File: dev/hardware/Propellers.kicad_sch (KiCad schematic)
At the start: 25 parts, among them J201 CPU PGMR, J202 GPU PGMR, J203 SPARE GPU HDR, J204 SPARE CPU HDR, SW201 CPU ~{RES}, SW202 GPU ~{RES}, SW203 DEBUG, U1 P8X32A-D40, Y1 6.5MHz

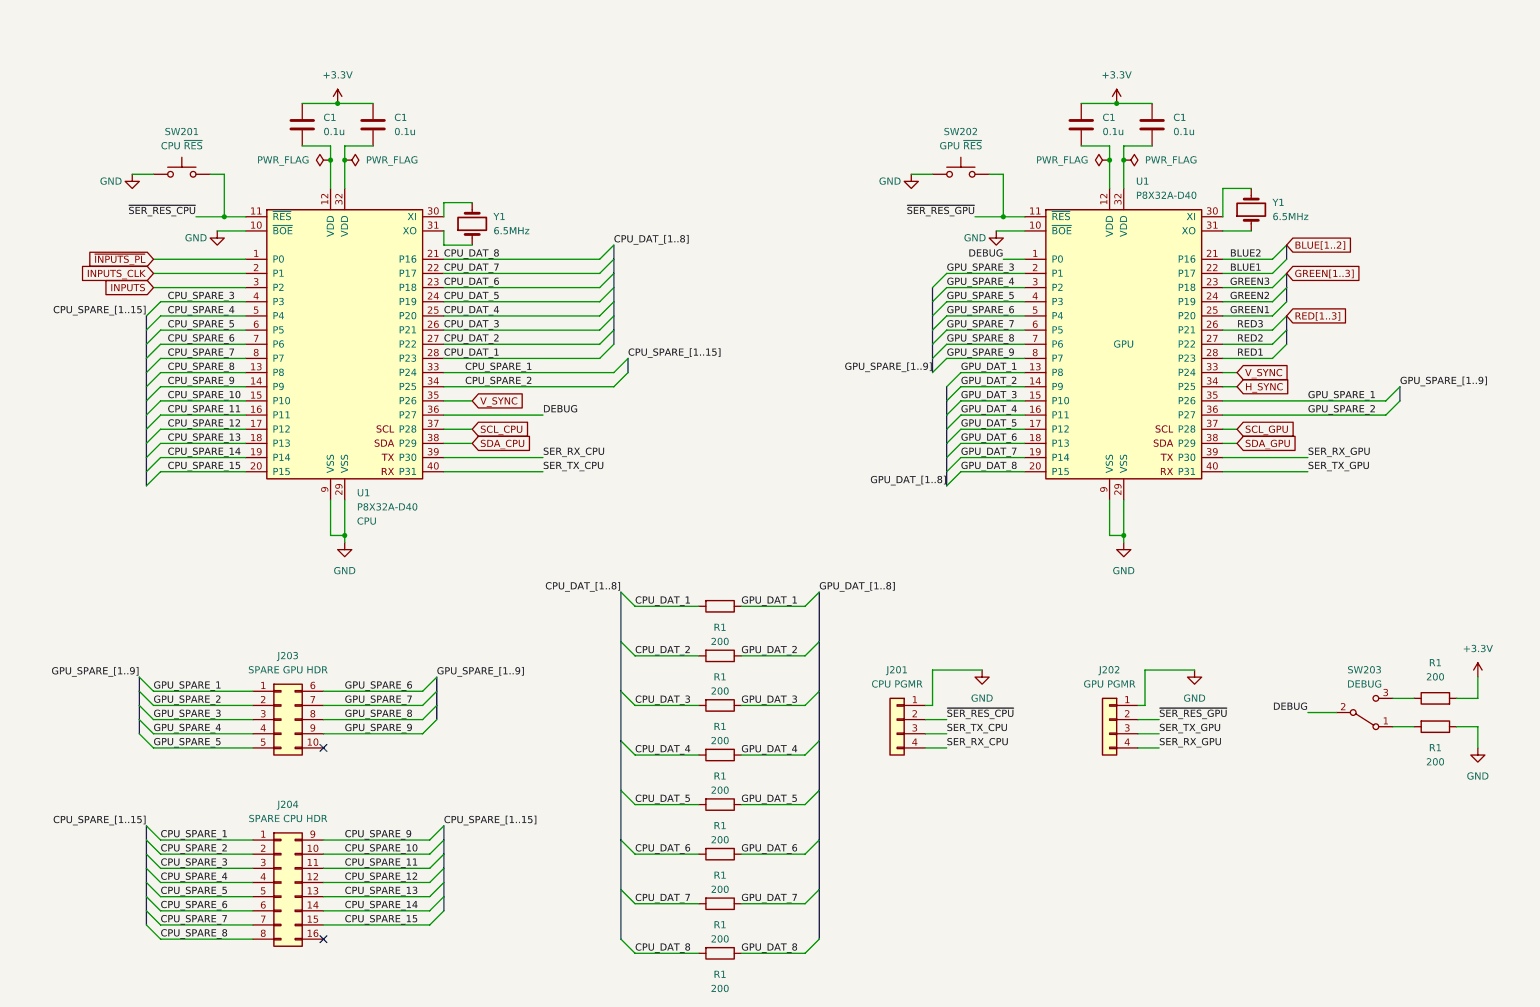
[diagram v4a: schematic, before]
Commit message: Updated netclasses and PCB specs
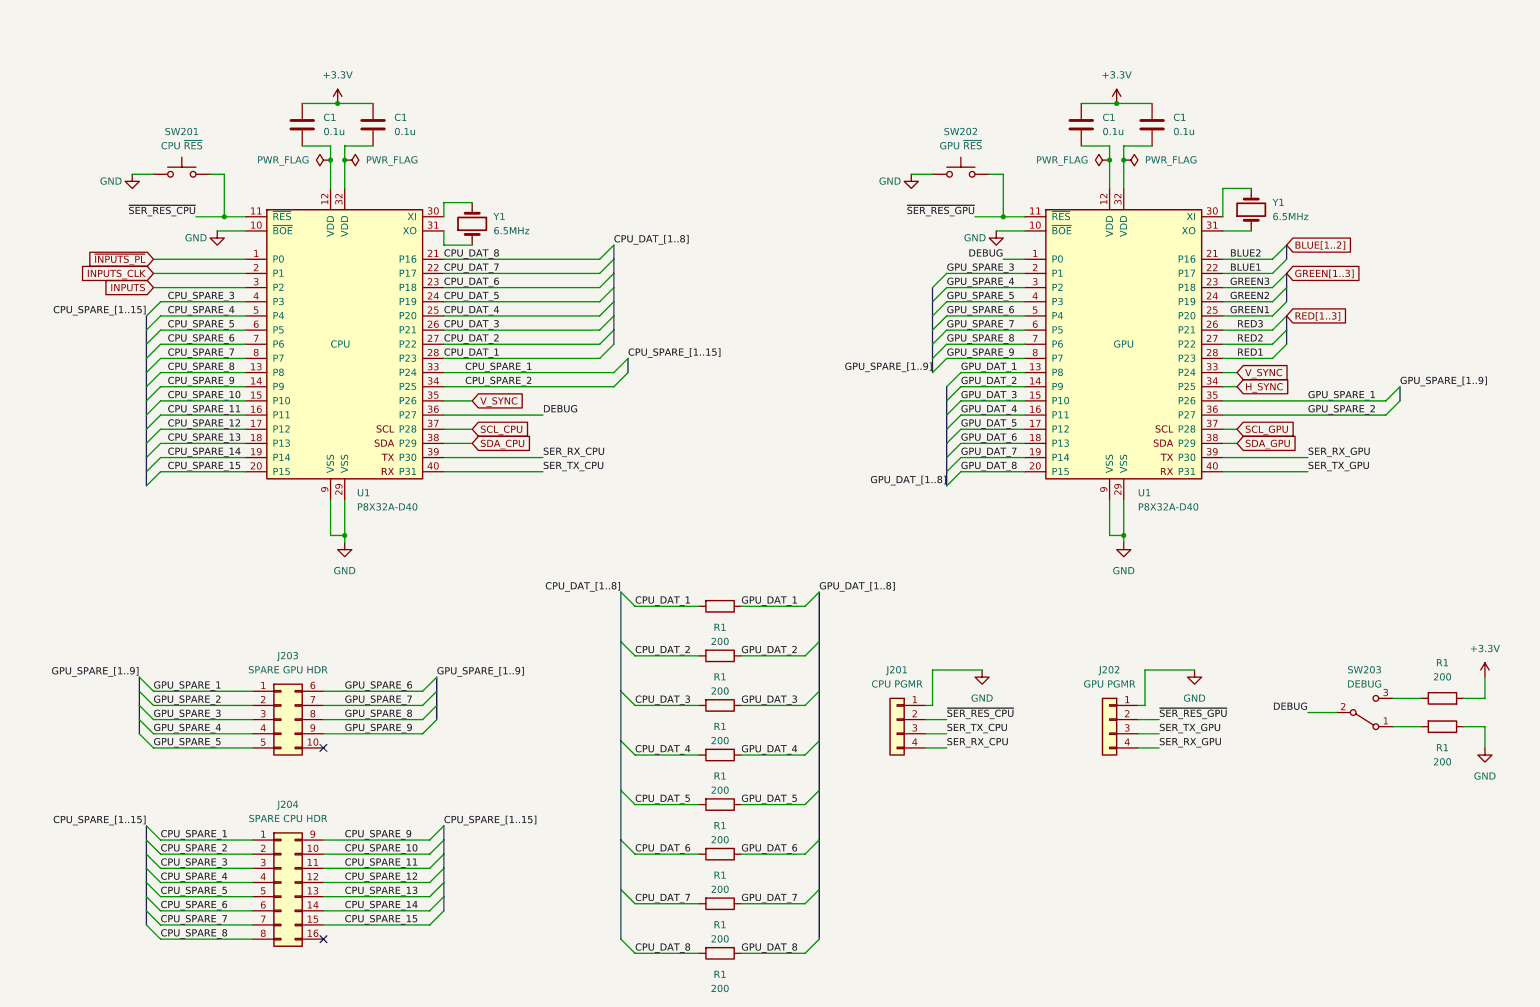
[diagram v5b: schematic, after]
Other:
- moved on the sheet: R1
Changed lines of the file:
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@@
     (stroke (width 0) (type default))
   )
-  (wire (pts (xy 261.62 139.7) (xy 265.43 139.7))
+  (wire (pts (xy 261.62 139.7) (xy 266.7 139.7))
     (stroke (width 0) (type default))
   )
@@
     (stroke (width 0) (type default))
   )
-  (wire (pts (xy 276.86 134.62) (xy 273.05 134.62))
+  (wire (pts (xy 278.13 134.62) (xy 274.32 134.62))
     (stroke (width 0) (type default))
   )
@@
     (stroke (width 0) (type default))
   )
-  (wire (pts (xy 276.86 143.51) (xy 276.86 139.7))
+  (wire (pts (xy 278.13 143.51) (xy 278.13 139.7))
     (stroke (width 0) (type default))
   )
@@
     (stroke (width 0) (type default))
   )
-  (wire (pts (xy 276.86 139.7) (xy 273.05 139.7))
+  (wire (pts (xy 278.13 139.7) (xy 274.32 139.7))
     (stroke (width 0) (type default))
   )
@@
     (stroke (width 0) (type default))
   )
-  (wire (pts (xy 276.86 130.81) (xy 276.86 134.62))
+  (wire (pts (xy 278.13 130.81) (xy 278.13 134.62))
     (stroke (width 0) (type default))
   )
@@
     (stroke (width 0) (type default))
   )
-  (wire (pts (xy 261.62 134.62) (xy 265.43 134.62))
+  (wire (pts (xy 261.62 134.62) (xy 266.7 134.62))
     (stroke (width 0) (type default))
   )
@@
     (property "Intersheetrefs" "${INTERSHEET_REFS}" (at 107.8509 86.36 0)
       (effects (font (size 1.27 1.27)) (justify left) hide)
+    )
+  )
+  (netclass_flag "" (length 1) (shape dot) (at 210.82 40.64 90) (fields_autoplaced)
+    (effects (font (size 1.27 1.27) (color 255 0 0 1)) (justify left bottom))
+    (property "Netclass" "Power" (at 209.82 39.9415 90)
+      (effects (font (size 1.27 1.27) italic) (justify left) hide)
+    )
+  )
+  (netclass_flag "" (length 1) (shape dot) (at 93.98 45.72 0) (fields_autoplaced)
+    (effects (font (size 1.27 1.27)) (justify left bottom))
+    (property "Netclass" "Signal" (at 94.6785 44.72 0)
+      (effects (font (size 1.27 1.27) italic) (justify left) hide)
+    )
+  )
+  (netclass_flag "" (length 1) (shape dot) (at 233.68 43.18 0) (fields_autoplaced)
+    (effects (font (size 1.27 1.27)) (justify left bottom))
+    (property "Netclass" "Signal" (at 234.3785 42.18 0)
+      (effects (font (size 1.27 1.27) italic) (justify left) hide)
+    )
+  )
+  (netclass_flag "" (length 1) (shape dot) (at 264.16 134.62 0) (fields_autoplaced)
+    (effects (font (size 1.27 1.27)) (justify left bottom))
+    (property "Netclass" "Signal" (at 264.8585 133.62 0)
+      (effects (font (size 1.27 1.27) italic) (justify left) hide)
+    )
+  )
+  (netclass_flag "" (length 1) (shape dot) (at 73.66 40.64 270) (fields_autoplaced)
+    (effects (font (size 1.27 1.27) (color 255 0 0 1)) (justify right bottom))
+    (property "Netclass" "Power" (at 74.66 39.9415 90)
+      (effects (font (size 1.27 1.27) italic) (justify left) hide)
+    )
+  )
+  (netclass_flag "" (length 1) (shape dot) (at 213.36 40.64 270) (fields_autoplaced)
+    (effects (font (size 1.27 1.27) (color 255 0 0 1)) (justify right bottom))
+    (property "Netclass" "Power" (at 214.36 39.9415 90)
+      (effects (font (size 1.27 1.27) italic) (justify left) hide)
+    )
+  )
+  (netclass_flag "" (length 1) (shape dot) (at 71.12 40.64 90) (fields_autoplaced)
+    (effects (font (size 1.27 1.27) (color 255 0 0 1)) (justify left bottom))
+    (property "Netclass" "Power" (at 70.12 39.9415 90)
+      (effects (font (size 1.27 1.27) italic) (justify left) hide)
+    )
+  )
+  (netclass_flag "" (length 1) (shape dot) (at 264.16 139.7 180) (fields_autoplaced)
+    (effects (font (size 1.27 1.27)) (justify right bottom))
+    (property "Netclass" "Signal" (at 264.8585 140.7 0)
+      (effects (font (size 1.27 1.27) italic) (justify left) hide)
     )
   )
@@
   )
   (symbol (lib_id "MCU_Parallax:P8X32A-D40") (at 213.36 71.12 0) (unit 1)
-    (in_bom yes) (on_board yes) (dnp no) (fields_autoplaced)
-    (property "Reference" "U1" (at 215.5541 41.91 0)
+    (in_bom yes) (on_board yes) (dnp no)
+    (property "Reference" "U1" (at 215.9 97.79 0)
       (effects (font (size 1.27 1.27)) (justify left))
     )
-    (property "Value" "P8X32A-D40" (at 215.5541 44.45 0)
+    (property "Value" "P8X32A-D40" (at 215.9 100.33 0)
       (effects (font (size 1.27 1.27)) (justify left))
     )
@@
         )
         (path "/7fc25e9e-3600-419b-89ef-b962e4e374c1/203ea849-2dbb-4e64-89c6-7fa05a05e11f"
-          (reference "Y1") (unit 1)
+          (reference "Y101") (unit 1)
         )
       )
@@
         )
         (path "/7fc25e9e-3600-419b-89ef-b962e4e374c1/203ea849-2dbb-4e64-89c6-7fa05a05e11f"
-          (reference "C1") (unit 1)
+          (reference "C204") (unit 1)
         )
       )
@@
     )
   )
-  (symbol (lib_id "power:+3.3V") (at 276.86 130.81 0) (unit 1)
-    (in_bom yes) (on_board yes) (dnp no) (fields_autoplaced)
-    (property "Reference" "#PWR0210" (at 276.86 134.62 0)
-      (effects (font (size 1.27 1.27)) hide)
-    )
-    (property "Value" "+3.3V" (at 276.86 125.73 0)
-      (effects (font (size 1.27 1.27)))
-    )
-    (property "Footprint" "" (at 276.86 130.81 0)
-      (effects (font (size 1.27 1.27)) hide)
-    )
-    (property "Datasheet" "" (at 276.86 130.81 0)
+  (symbol (lib_id "power:+3.3V") (at 278.13 130.81 0) (unit 1)
+    (in_bom yes) (on_board yes) (dnp no) (fields_autoplaced)
+    (property "Reference" "#PWR0210" (at 278.13 134.62 0)
+      (effects (font (size 1.27 1.27)) hide)
+    )
+    (property "Value" "+3.3V" (at 278.13 125.73 0)
+      (effects (font (size 1.27 1.27)))
+    )
+    (property "Footprint" "" (at 278.13 130.81 0)
+      (effects (font (size 1.27 1.27)) hide)
+    )
+    (property "Datasheet" "" (at 278.13 130.81 0)
       (effects (font (size 1.27 1.27)) hide)
     )
@@
     )
   )
-  (symbol (lib_id "Device:R") (at 269.24 139.7 270) (unit 1)
-    (in_bom yes) (on_board yes) (dnp no) (fields_autoplaced)
-    (property "Reference" "R1" (at 269.24 143.51 90)
-      (effects (font (size 1.27 1.27)))
-    )
-    (property "Value" "200" (at 269.24 146.05 90)
-      (effects (font (size 1.27 1.27)))
-    )
-    (property "Footprint" "Resistor_THT:R_Axial_DIN0207_L6.3mm_D2.5mm_P10.16mm_Horizontal" (at 269.24 137.922 90)
-      (effects (font (size 1.27 1.27)) hide)
-    )
-    (property "Datasheet" "~" (at 269.24 139.7 0)
+  (symbol (lib_id "Device:R") (at 270.51 139.7 270) (unit 1)
+    (in_bom yes) (on_board yes) (dnp no) (fields_autoplaced)
+    (property "Reference" "R1" (at 270.51 143.51 90)
+      (effects (font (size 1.27 1.27)))
+    )
+    (property "Value" "200" (at 270.51 146.05 90)
+      (effects (font (size 1.27 1.27)))
+    )
+    (property "Footprint" "Resistor_THT:R_Axial_DIN0207_L6.3mm_D2.5mm_P10.16mm_Horizontal" (at 270.51 137.922 90)
+      (effects (font (size 1.27 1.27)) hide)
+    )
+    (property "Datasheet" "~" (at 270.51 139.7 0)
       (effects (font (size 1.27 1.27)) hide)
     )
@@
   )
   (symbol (lib_id "MCU_Parallax:P8X32A-D40") (at 73.66 71.12 0) (unit 1)
-    (in_bom yes) (on_board yes) (dnp no) (fields_autoplaced)
+    (in_bom yes) (on_board yes) (dnp no)
     (property "Reference" "U1" (at 75.8541 97.79 0)
       (effects (font (size 1.27 1.27)) (justify left))
@@
       (effects (font (size 1.27 1.27)) hide)
     )
-    (property "Role" "CPU" (at 75.8541 102.87 0)
+    (property "Role" "CPU" (at 71.12 71.12 0)
       (effects (font (size 1.27 1.27)) (justify left))
     )
@@
     )
   )
-  (symbol (lib_id "power:GND") (at 276.86 143.51 0) (unit 1)
-    (in_bom yes) (on_board yes) (dnp no) (fields_autoplaced)
-    (property "Reference" "#PWR0209" (at 276.86 149.86 0)
-      (effects (font (size 1.27 1.27)) hide)
-    )
-    (property "Value" "GND" (at 276.86 148.59 0)
-      (effects (font (size 1.27 1.27)))
-    )
-    (property "Footprint" "" (at 276.86 143.51 0)
-      (effects (font (size 1.27 1.27)) hide)
-    )
-    (property "Datasheet" "" (at 276.86 143.51 0)
+  (symbol (lib_id "power:GND") (at 278.13 143.51 0) (unit 1)
+    (in_bom yes) (on_board yes) (dnp no) (fields_autoplaced)
+    (property "Reference" "#PWR0209" (at 278.13 149.86 0)
+      (effects (font (size 1.27 1.27)) hide)
+    )
+    (property "Value" "GND" (at 278.13 148.59 0)
+      (effects (font (size 1.27 1.27)))
+    )
+    (property "Footprint" "" (at 278.13 143.51 0)
+      (effects (font (size 1.27 1.27)) hide)
+    )
+    (property "Datasheet" "" (at 278.13 143.51 0)
       (effects (font (size 1.27 1.27)) hide)
     )
@@
     )
   )
-  (symbol (lib_id "Device:R") (at 269.24 134.62 90) (unit 1)
-    (in_bom yes) (on_board yes) (dnp no) (fields_autoplaced)
-    (property "Reference" "R1" (at 269.24 128.27 90)
-      (effects (font (size 1.27 1.27)))
-    )
-    (property "Value" "200" (at 269.24 130.81 90)
-      (effects (font (size 1.27 1.27)))
-    )
-    (property "Footprint" "Resistor_THT:R_Axial_DIN0207_L6.3mm_D2.5mm_P10.16mm_Horizontal" (at 269.24 136.398 90)
-      (effects (font (size 1.27 1.27)) hide)
-    )
-    (property "Datasheet" "~" (at 269.24 134.62 0)
-      (effects (font (size 1.27 1.27)) hide)
-    )
+  (symbol (lib_id "Device:R") (at 270.51 134.62 90) (unit 1)
+    (in_bom yes) (on_board yes) (dnp no) (fields_autoplaced)
+    (property "Reference" "R1" (at 270.51 128.27 90)
+      (effects (font (size 1.27 1.27)))
+    )
+    (property "Value" "200" (at 270.51 130.81 90)
+      (effects (font (size 1.27 1.27)))
+    )
+    (property "Footprint" "Resistor_THT:R_Axial_DIN0207_L6.3mm_D2.5mm_P10.16mm_Horizontal" (at 270.51 136.398 90)
+      (effects (font (size 1.27 1.27)) hide)
+    )
+    (property "Datasheet" "~" (at 270.51 134.62 0)
+      (effects (font (size 1.27 1.27)) hide)
+    )
